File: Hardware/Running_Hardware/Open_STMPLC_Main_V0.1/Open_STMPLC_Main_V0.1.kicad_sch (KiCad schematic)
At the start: 4 parts

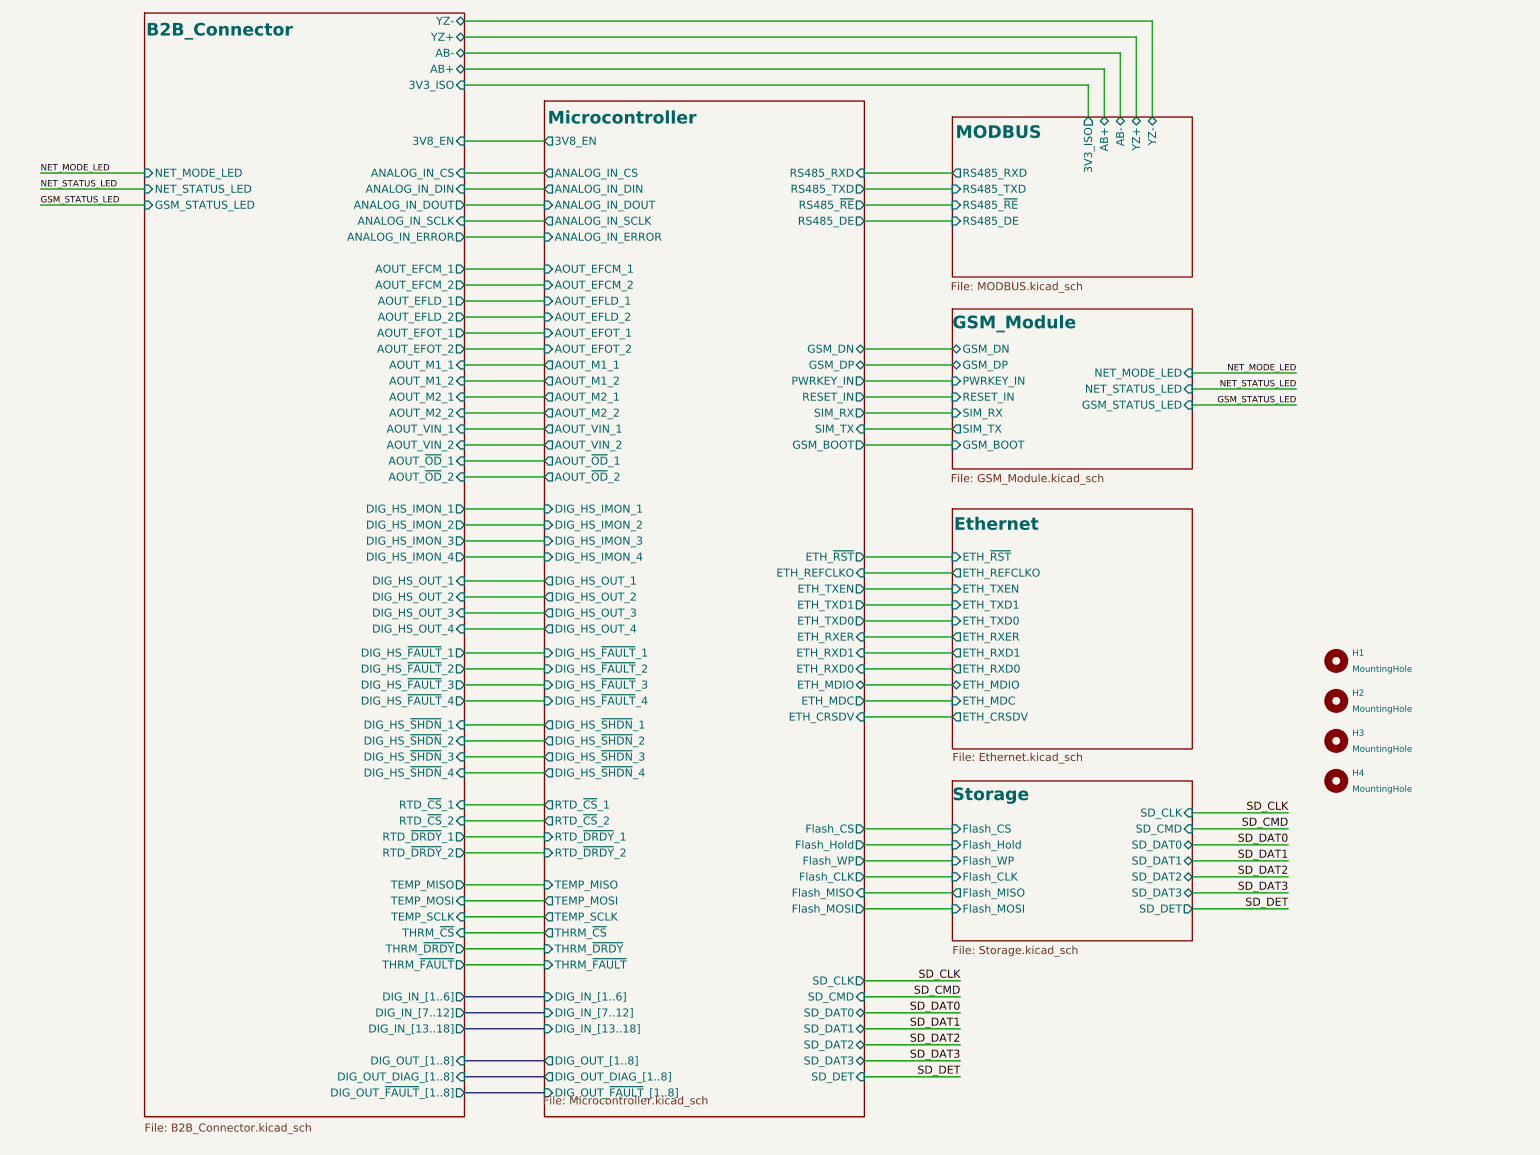
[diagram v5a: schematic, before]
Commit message: Pin mapping - MCU connectors
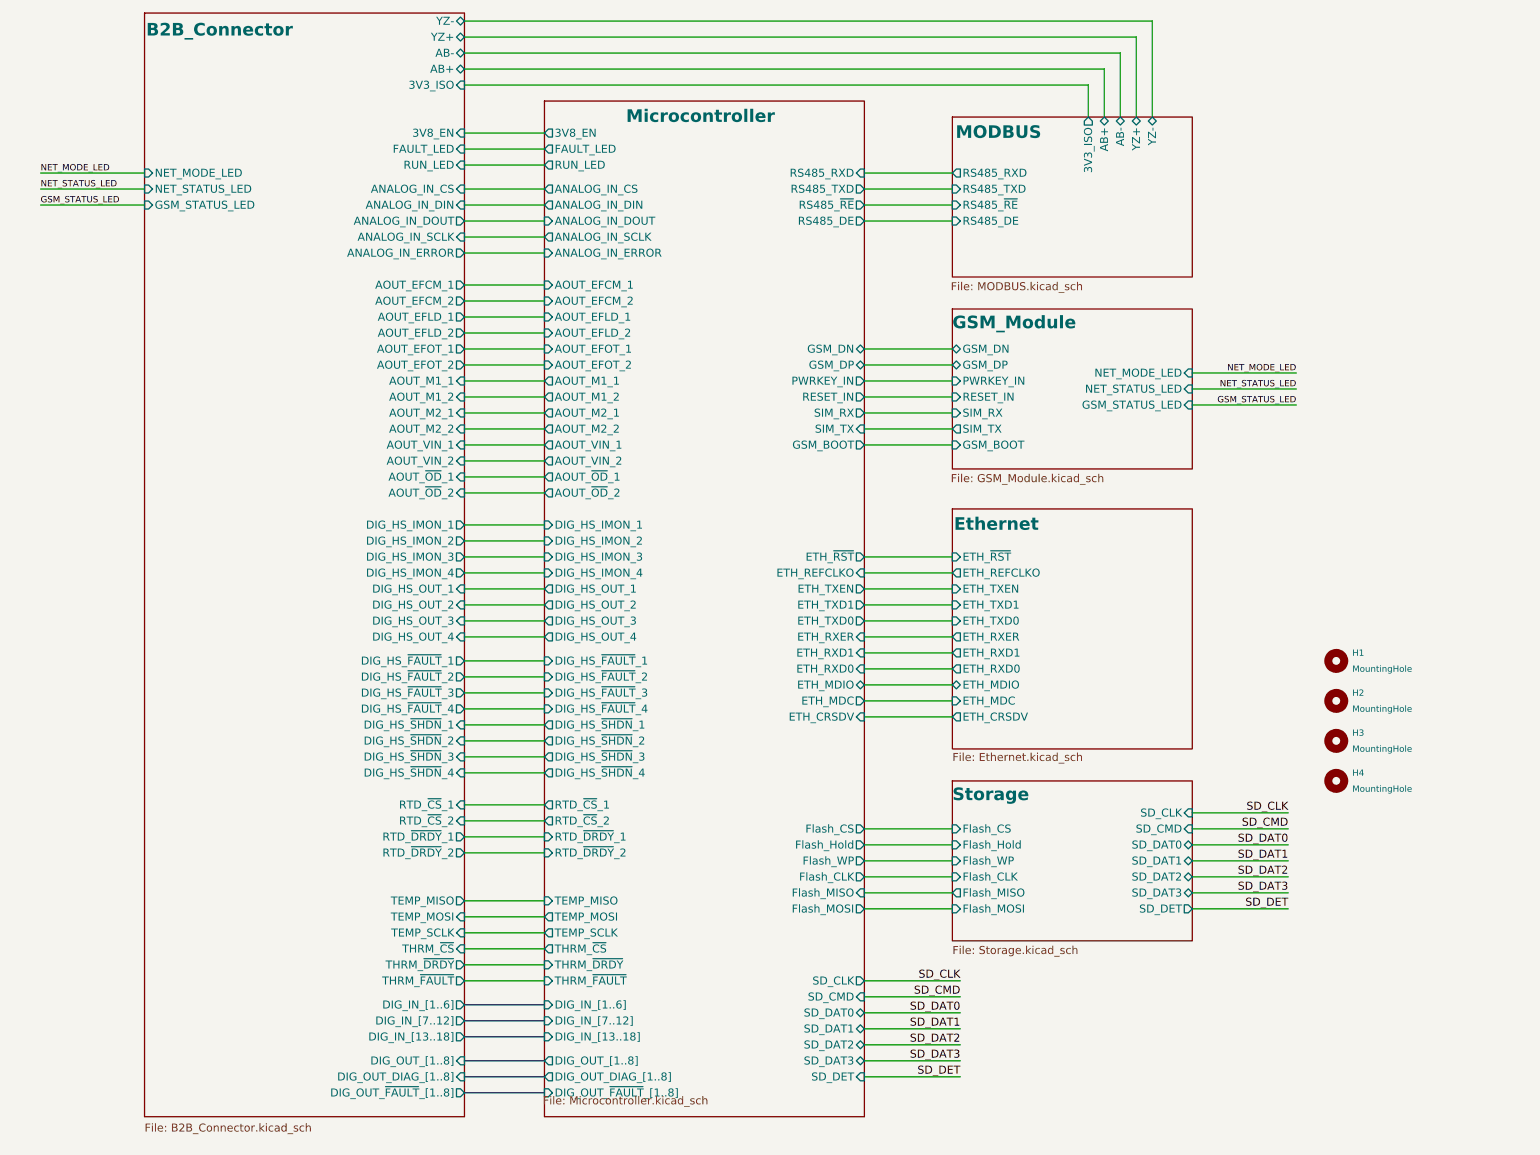
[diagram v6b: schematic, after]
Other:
- sheet B2B_Connector ports: added FAULT_LED, RUN_LED; removed none
- sheet Microcontroller ports: added FAULT_LED, RUN_LED; removed none

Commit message: PCB routing completion v0.1 Main
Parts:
- added FID1, FID2, FID3, FID4: Fiducial, Fiducial:Fiducial_1mm_Mask3mm, symbol Mechanical:Fiducial
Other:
- sheet Ethernet ports: added none; removed ETH_RXER
- sheet Microcontroller ports: added none; removed ETH_RXER

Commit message: Silkscreen and DRC
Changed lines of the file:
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@@
 	(title_block
 		(title "Open_STMPLC_Main")
-		(date "2026-05-23")
+		(date "2026-05-24")
 		(rev "0.1")
 	)
@@
 		(effects
 			(font
-				(size 1.27 1.27)
+				(size 1 1)
 			)
 			(justify right bottom)
@@
 		(effects
 			(font
-				(size 1.27 1.27)
+				(size 1 1)
 			)
 			(justify right bottom)
@@
 		(effects
 			(font
-				(size 1.27 1.27)
+				(size 1 1)
 			)
 			(justify right bottom)
@@
 		(effects
 			(font
-				(size 1.27 1.27)
+				(size 1 1)
 			)
 			(justify right bottom)
@@
 		(effects
 			(font
-				(size 1.27 1.27)
+				(size 1 1)
 			)
 			(justify right bottom)
@@
 		(effects
 			(font
-				(size 1.27 1.27)
+				(size 1 1)
 			)
 			(justify right bottom)
@@
 		(effects
 			(font
-				(size 1.27 1.27)
+				(size 1 1)
 			)
 			(justify right bottom)
@@
 		(effects
 			(font
-				(size 1.27 1.27)
+				(size 1 1)
 			)
 			(justify right bottom)
@@
 		(effects
 			(font
-				(size 1.27 1.27)
+				(size 1 1)
 			)
 			(justify right bottom)
@@
 		(effects
 			(font
-				(size 1.27 1.27)
+				(size 1 1)
 			)
 			(justify right bottom)
@@
 		(effects
 			(font
-				(size 1.27 1.27)
+				(size 1 1)
 			)
 			(justify right bottom)
@@
 		(effects
 			(font
-				(size 1.27 1.27)
+				(size 1 1)
 			)
 			(justify right bottom)
@@
 		(effects
 			(font
-				(size 1.27 1.27)
+				(size 1 1)
 			)
 			(justify right bottom)
@@
 		(effects
 			(font
-				(size 1.27 1.27)
+				(size 1 1)
 			)
 			(justify right bottom)
@@
 			(effects
 				(font
-					(size 1.27 1.27)
+					(size 1 1)
 				)
 				(justify left)
@@
 			(effects
 				(font
-					(size 1.27 1.27)
+					(size 1 1)
 				)
 				(justify left)
@@
 			(effects
 				(font
-					(size 1.27 1.27)
+					(size 1 1)
 				)
 				(justify left)
@@
 			(effects
 				(font
-					(size 1.27 1.27)
+					(size 1 1)
 				)
 				(justify left)
@@
 			(effects
 				(font
-					(size 1.27 1.27)
+					(size 1 1)
 				)
 				(justify left)
@@
 			(effects
 				(font
-					(size 1.27 1.27)
+					(size 1 1)
 				)
 				(justify left)
@@
 			(effects
 				(font
-					(size 1.27 1.27)
+					(size 1 1)
 				)
 				(justify left)
@@
 			(effects
 				(font
-					(size 1.27 1.27)
+					(size 1 1)
 				)
 				(justify left)
